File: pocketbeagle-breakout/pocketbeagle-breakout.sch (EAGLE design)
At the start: 89 parts, among them J30 4-1734592-04-1734592-0, J31 4-1734592-04-1734592-0, J5 POWER_JACKSLT, P1 BCS-118-L-D-TE, P1IN BCS-118-L-D-TE, P2 BCS-118-L-D-TE, P2IN BCS-118-L-D-TE, U1 TCAN330

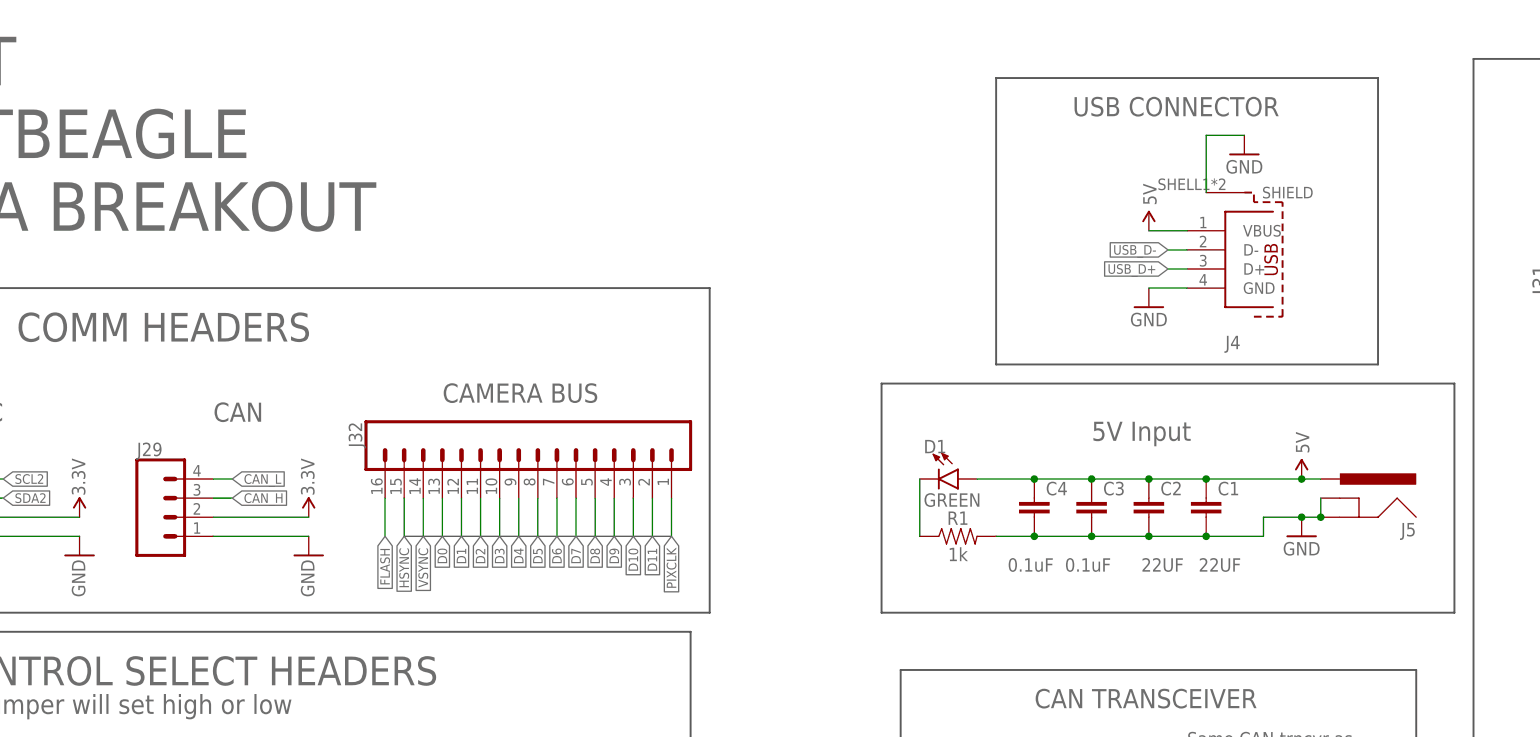
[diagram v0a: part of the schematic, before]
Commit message: address review comments: used round hole on USB and power, changed CAN connector, other small stuff
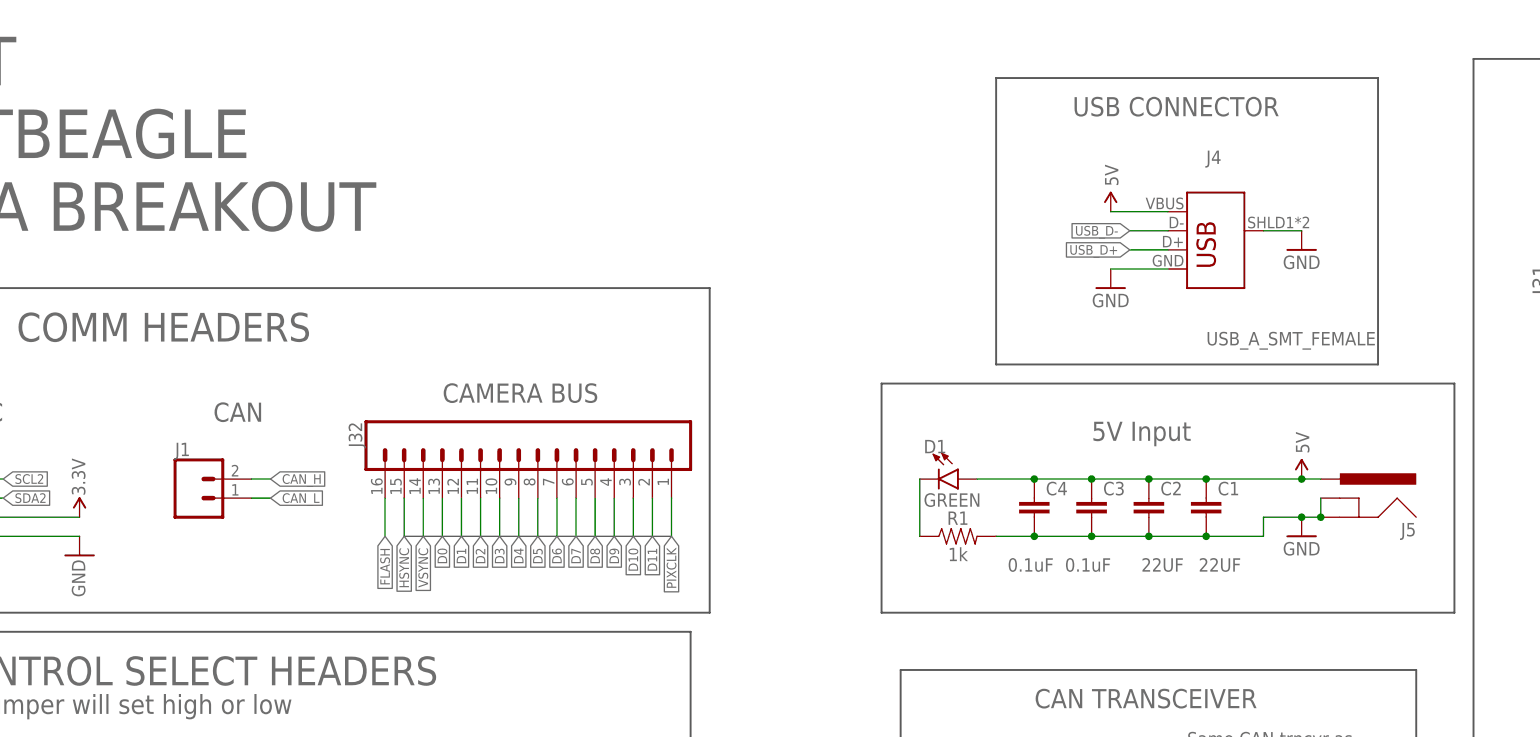
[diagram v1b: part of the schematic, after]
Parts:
- removed J29: (no value), SparkFun-Connectors:CONN_041X04_NO_SILK
- added J1: (no value), SparkFun-Connectors:CONN_025MM
- J4: value (none) -> USB_A_SMT_FEMALE; device J-WURTH-USB-A-FEMALE-629104151021:USB-A-FEMALE-SMD -> SparkFun-Connectors:USB_A_SMT_FEMALE
- J5: value POWER_JACKSLT -> POWER_JACK; device SparkFun-Connectors:POWER_JACKSLT -> SparkFun-Connectors:POWER_JACK
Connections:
- net 3.3V: no longer J29.2
- net CAN_H: now also J1.2; no longer J29.3
- net CAN_L: now also J1.1; no longer J29.4
- net GND: no longer J29.1
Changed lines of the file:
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@@
 <part name="P1IN" library="J-SAMTEC-2x18-BCS-118-L-D-TE" deviceset="BCS-118-L-D-TE" device=""/>
 <part name="P2IN" library="J-SAMTEC-2x18-BCS-118-L-D-TE" deviceset="BCS-118-L-D-TE" device=""/>
-<part name="J4" library="J-WURTH-USB-A-FEMALE-629104151021" deviceset="USB-A-FEMALE-SMD" device="" package3d_urn="urn:adsk.eagle:package:2054430/3"/>
-<part name="J5" library="SparkFun-Connectors" deviceset="POWER_JACK" device="SLT" package3d_urn="urn:adsk.eagle:package:38222/1"/>
+<part name="J4" library="SparkFun-Connectors" deviceset="USB_A" device="_SMT_FEMALE" package3d_urn="urn:adsk.eagle:package:38297/1"/>
+<part name="J5" library="SparkFun-Connectors" deviceset="POWER_JACK" device="" package3d_urn="urn:adsk.eagle:package:38231/1" value="POWER_JACK"/>
 <part name="C1" library="SparkFun-Capacitors" deviceset="22UF" device="-1210-16V-20%" value="22UF"/>
 <part name="C2" library="SparkFun-Capacitors" deviceset="22UF" device="-1210-16V-20%" value="22UF"/>
@@
 <part name="GND41" library="SparkFun-PowerSymbols" deviceset="GND" device=""/>
 <part name="C4" library="SparkFun-Capacitors" deviceset="0.1UF" device="-0603-100V-10%" value="0.1uF"/>
-<part name="J29" library="SparkFun-Connectors" deviceset="CONN_04" device="1X04_NO_SILK" package3d_urn="urn:adsk.eagle:package:38094/1"/>
 <part name="SJ1" library="SparkFun-Passives" deviceset="SOLDERJUMPER" device="NC2" value="SOLDERJUMPERNC2"/>
 <part name="SJ2" library="SparkFun-Passives" deviceset="SOLDERJUMPER" device="NC2" value="SOLDERJUMPERNC2"/>
@@
 <part name="SJ16" library="SparkFun-Passives" deviceset="SOLDERJUMPER" device="NC2" value="SOLDERJUMPERNC2"/>
 <part name="U1" library="U-TI-TCAN330-CAN-transceiver" deviceset="TCAN330" device=""/>
-<part name="GND47" library="SparkFun-PowerSymbols" deviceset="GND" device=""/>
-<part name="SUPPLY32" library="SparkFun-PowerSymbols" deviceset="3.3V" device=""/>
 <part name="SUPPLY33" library="SparkFun-PowerSymbols" deviceset="3.3V" device=""/>
 <part name="GND48" library="SparkFun-PowerSymbols" deviceset="GND" device=""/>
@@
 <part name="SUPPLY1" library="SparkFun-PowerSymbols" deviceset="5V" device=""/>
 <part name="SUPPLY2" library="SparkFun-PowerSymbols" deviceset="5V" device=""/>
+<part name="J1" library="SparkFun-Connectors" deviceset="CONN_02" device="5MM" package3d_urn="urn:adsk.eagle:package:38044/1"/>
 </parts>
 <sheets>
@@
 <attribute name="NAME" x="347.0656" y="127.2286" size="2.0828" layer="95" ratio="6" rot="SR0"/>
 </instance>
-<instance part="J4" gate="G$1" x="241.3" y="264.16" smashed="yes" rot="MR180">
-<attribute name="NAME" x="238.76" y="252.73" size="1.778" layer="95" rot="MR180"/>
-<attribute name="VALUE" x="238.76" y="276.86" size="1.778" layer="96" rot="MR180"/>
+<instance part="J4" gate="G$1" x="238.76" y="264.16" smashed="yes">
+<attribute name="NAME" x="236.22" y="275.59" size="1.778" layer="95"/>
+<attribute name="VALUE" x="236.22" y="251.46" size="1.778" layer="96"/>
 </instance>
 <instance part="J5" gate="G$1" x="254" y="236.22" smashed="yes" rot="MR0">
@@
 <attribute name="VALUE" x="290.83" y="99.06" size="1.778" layer="96" rot="R180" align="top-center"/>
 </instance>
-<instance part="GND26" gate="1" x="228.6" y="256.54" smashed="yes">
-<attribute name="VALUE" x="228.6" y="254" size="1.778" layer="96" rot="R180" align="top-center"/>
-</instance>
-<instance part="SUPPLY20" gate="G$1" x="228.6" y="266.7" smashed="yes">
-<attribute name="VALUE" x="229.616" y="271.526" size="1.778" layer="96" rot="R90" align="bottom-center"/>
-</instance>
-<instance part="GND27" gate="1" x="241.3" y="276.86" smashed="yes">
-<attribute name="VALUE" x="241.3" y="274.32" size="1.778" layer="96" rot="R180" align="top-center"/>
+<instance part="GND26" gate="1" x="223.52" y="259.08" smashed="yes">
+<attribute name="VALUE" x="223.52" y="256.54" size="1.778" layer="96" rot="R180" align="top-center"/>
+</instance>
+<instance part="SUPPLY20" gate="G$1" x="223.52" y="269.24" smashed="yes">
+<attribute name="VALUE" x="224.536" y="274.066" size="1.778" layer="96" rot="R90" align="bottom-center"/>
+</instance>
+<instance part="GND27" gate="1" x="248.92" y="264.16" smashed="yes">
+<attribute name="VALUE" x="248.92" y="261.62" size="1.778" layer="96" rot="R180" align="top-center"/>
 </instance>
 <instance part="GND28" gate="1" x="248.92" y="226.06" smashed="yes">
@@
 <attribute name="NAME" x="214.884" y="231.521" size="1.778" layer="95" font="vector"/>
 <attribute name="VALUE" x="209.804" y="221.361" size="1.778" layer="96" font="vector"/>
-</instance>
-<instance part="J29" gate="G$1" x="99.06" y="228.6" smashed="yes">
-<attribute name="VALUE" x="93.98" y="221.234" size="1.778" layer="96" font="vector"/>
-<attribute name="NAME" x="93.98" y="236.728" size="1.778" layer="95" font="vector"/>
 </instance>
 <instance part="SJ1" gate="1" x="365.76" y="246.38" smashed="yes" rot="R90"/>
@@
 <attribute name="VALUE" x="236.22" y="152.4" size="1.778" layer="96"/>
 </instance>
-<instance part="GND47" gate="1" x="116.84" y="223.52" smashed="yes">
-<attribute name="VALUE" x="115.824" y="220.472" size="1.778" layer="96" rot="R90" align="top-center"/>
-</instance>
-<instance part="SUPPLY32" gate="G$1" x="116.84" y="228.6" smashed="yes">
-<attribute name="VALUE" x="117.602" y="233.934" size="1.778" layer="96" rot="R90" align="bottom-center"/>
-</instance>
 <instance part="SUPPLY33" gate="G$1" x="228.6" y="190.5" smashed="yes">
 <attribute name="VALUE" x="229.362" y="195.834" size="1.778" layer="96" rot="R90" align="bottom-center"/>
@@
 <attribute name="VALUE" x="282.702" y="251.206" size="1.778" layer="96" rot="R90" align="bottom-center"/>
 </instance>
+<instance part="J1" gate="G$1" x="101.6" y="231.14" smashed="yes">
+<attribute name="VALUE" x="99.06" y="226.314" size="1.778" layer="96" font="vector"/>
+<attribute name="NAME" x="99.06" y="236.728" size="1.778" layer="95" font="vector"/>
+</instance>
 </instances>
 <busses>
@@
 <pinref part="J4" gate="G$1" pin="GND"/>
 <pinref part="GND26" gate="1" pin="GND"/>
-<wire x1="233.68" y1="259.08" x2="228.6" y2="259.08" width="0.1524" layer="91"/>
+<wire x1="231.14" y1="261.62" x2="223.52" y2="261.62" width="0.1524" layer="91"/>
 </segment>
 <segment>
 <pinref part="GND27" gate="1" pin="GND"/>
-<wire x1="241.3" y1="279.4" x2="236.22" y2="279.4" width="0.1524" layer="91"/>
+<wire x1="248.92" y1="266.7" x2="243.84" y2="266.7" width="0.1524" layer="91"/>
 <pinref part="J4" gate="G$1" pin="SHIELD"/>
-<wire x1="236.22" y1="279.4" x2="236.22" y2="271.78" width="0.1524" layer="91"/>
 </segment>
 <segment>
@@
 </segment>
 <segment>
-<pinref part="J29" gate="G$1" pin="1"/>
-<pinref part="GND47" gate="1" pin="GND"/>
-<wire x1="104.14" y1="226.06" x2="116.84" y2="226.06" width="0.1524" layer="91"/>
-</segment>
-<segment>
 <pinref part="U1" gate="G$1" pin="GND"/>
 <pinref part="GND48" gate="1" pin="GND"/>
@@
 <pinref part="J4" gate="G$1" pin="VBUS"/>
 <pinref part="SUPPLY20" gate="G$1" pin="5V"/>
-<wire x1="233.68" y1="266.7" x2="228.6" y2="266.7" width="0.1524" layer="91"/>
+<wire x1="231.14" y1="269.24" x2="223.52" y2="269.24" width="0.1524" layer="91"/>
 </segment>
 <segment>
@@
 </segment>
 <segment>
-<pinref part="J29" gate="G$1" pin="2"/>
-<pinref part="SUPPLY32" gate="G$1" pin="3.3V"/>
-<wire x1="104.14" y1="228.6" x2="116.84" y2="228.6" width="0.1524" layer="91"/>
-</segment>
-<segment>
 <pinref part="SUPPLY33" gate="G$1" pin="3.3V"/>
 <pinref part="U1" gate="G$1" pin="VCC"/>
@@
 <segment>
 <pinref part="J4" gate="G$1" pin="D-"/>
-<wire x1="233.68" y1="264.16" x2="231.14" y2="264.16" width="0.1524" layer="91"/>
-<label x="231.14" y="264.16" size="1.27" layer="95" rot="R180" xref="yes"/>
+<wire x1="231.14" y1="266.7" x2="226.06" y2="266.7" width="0.1524" layer="91"/>
+<label x="226.06" y="266.7" size="1.27" layer="95" rot="R180" xref="yes"/>
 </segment>
 <segment>
@@
 <segment>
 <pinref part="J4" gate="G$1" pin="D+"/>
-<wire x1="233.68" y1="261.62" x2="231.14" y2="261.62" width="0.1524" layer="91"/>
-<label x="231.14" y="261.62" size="1.27" layer="95" rot="R180" xref="yes"/>
+<wire x1="231.14" y1="264.16" x2="226.06" y2="264.16" width="0.1524" layer="91"/>
+<label x="226.06" y="264.16" size="1.27" layer="95" rot="R180" xref="yes"/>
 </segment>
 <segment>
@@
 <net name="CAN_H" class="0">
 <segment>
-<pinref part="J29" gate="G$1" pin="3"/>
-<wire x1="104.14" y1="231.14" x2="106.68" y2="231.14" width="0.1524" layer="91"/>
-<label x="106.68" y="231.14" size="1.27" layer="95" xref="yes"/>
-</segment>
-<segment>
 <pinref part="U1" gate="G$1" pin="CANH"/>
 <wire x1="241.3" y1="175.26" x2="243.84" y2="175.26" width="0.1524" layer="91"/>
 <label x="243.84" y="175.26" size="1.27" layer="95" xref="yes"/>
 </segment>
+<segment>
+<pinref part="J1" gate="G$1" pin="2"/>
+<wire x1="109.22" y1="233.68" x2="111.76" y2="233.68" width="0.1524" layer="91"/>
+<label x="111.76" y="233.68" size="1.27" layer="95" xref="yes"/>
+</segment>
 </net>
 <net name="CAN_L" class="0">
-<segment>
-<pinref part="J29" gate="G$1" pin="4"/>
-<wire x1="104.14" y1="233.68" x2="106.68" y2="233.68" width="0.1524" layer="91"/>
-<label x="106.68" y="233.68" size="1.27" layer="95" xref="yes"/>
-</segment>
 <segment>
 <pinref part="U1" gate="G$1" pin="CANL"/>
@@
 <label x="243.84" y="170.18" size="1.27" layer="95" xref="yes"/>
 </segment>
-</net>
+<segment>
+<pinref part="J1" gate="G$1" pin="1"/>
+<wire x1="109.22" y1="231.14" x2="111.76" y2="231.14" width="0.1524" layer="91"/>
+<label x="111.76" y="231.14" size="1.27" layer="95" xref="yes"/>
+</segment>
+</net>

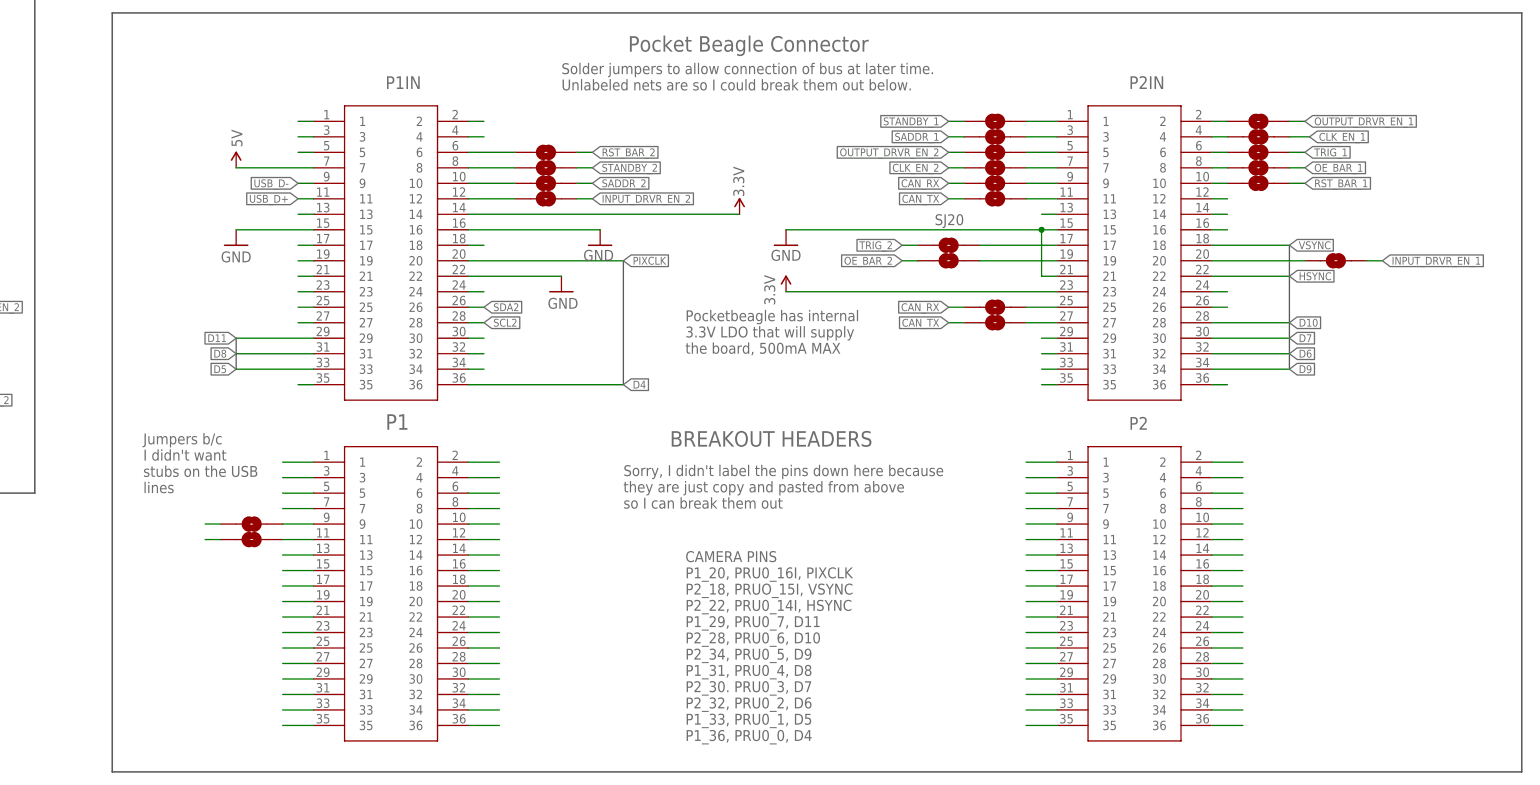
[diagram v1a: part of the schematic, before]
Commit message: Added labels, double checked breakouts, cleaned up ERCs and checked DRCs.
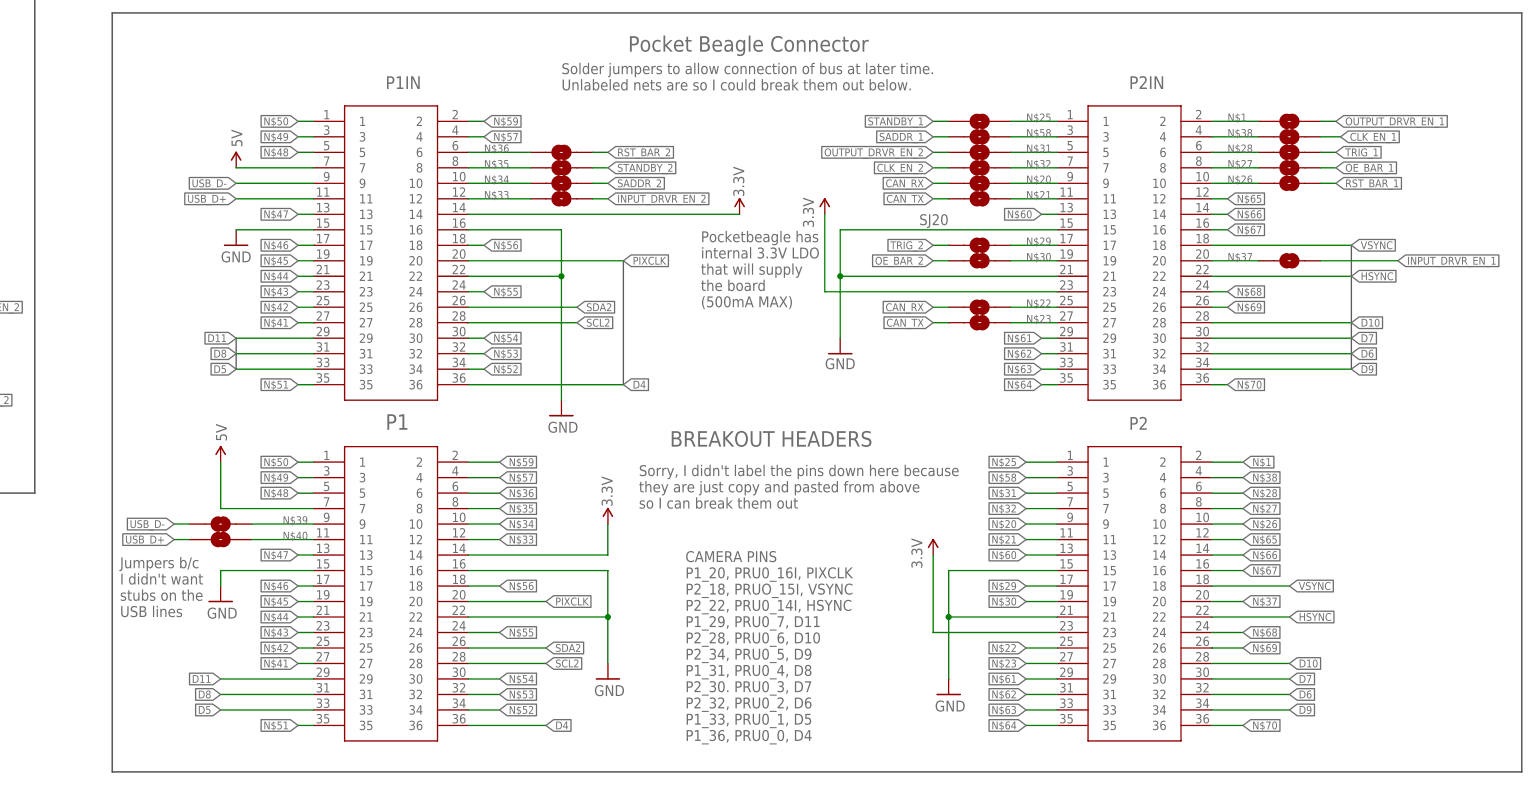
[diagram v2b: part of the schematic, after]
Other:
- note added: "Pocketbeagle has internal 3.3V LDO that will supply the board (500mA MAX)"
- note removed: "Pocketbeagle has internal 3.3V LDO that will supply the board, 500mA MAX"
- moved on the sheet: SJ20
